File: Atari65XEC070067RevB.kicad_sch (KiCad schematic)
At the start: 192 parts, among them J7 DIN-7, Q1 2N3904, Q2 2N3904, Q3 2N3904, Q4 2N3904, Q5 2N3904, Q6 2N3904, SW1 SW_SPDT, U1 LM358, U17 GTIA, U18 74LS08, U19 NE555P, U20 4050, U21 74LS74, U22 POKEY, U23 6520, U24 4051, U25 4051, U34 MMMU, U35 74LS95, U4 BASIC, U5 OS ROM, U6 SALLY, U7 ANTIC, Y2 4.33618MHz

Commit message: add ports
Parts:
- added C63, C64, C65, C66, C71, C72, C73, C74, C75, C76, C77, C78, C82, C83, C84, C85, C86, C87, C88, C89, C90, C91, C92, C96, C97: 1nF, symbol Device:C_Small
- added C68, C69, C70, C93: 100nF, symbol Device:C_Small
- added C94, C95: 10nF, symbol Device:C_Small
- added CR5: ~, symbol Device:D_Small
- added J1: SIO, symbol Library:SIO
- added J1: ~, symbol Library:KEYBOARD
- added J2: MONITOR, symbol Connector:DIN-5_180degree
- added J5, J6: JOY1, symbol Connector:DE9_Socket
- added L102, L23, L30, L31: FB, symbol Device:L_Ferrite
- added L14: 22uH, symbol Device:L_Ferrite
- added L15, L16, L17, L18, L19, L20, L21, L22, L24, L26, L27, L28, L29: 10uH, symbol Device:L_Ferrite
- added Q7: MPSA55, PCM_Package_TO_SOT_THT_AKL:TO-92_Inline_Wide_EBC, symbol PCM_Transistor_BJT_AKL:MPSA56
- added R117, R118, R119: 100R, symbol Device:R_Small
- added R120, R121, R122, R123, R124, R125, R126, R127, R132, R133, R134, R135, R136, R95: 220R, symbol Device:R_Small
- added R128, R129, R130, R131, R90: 100, symbol Device:R_Small
- added R137, R138, R139, R140, R141, R142, R143, R144, R145, R146, R147, R148, R149, R150, R151, R152, R153: 270R, symbol Device:R_Small
- added R205: 150R, symbol Device:R_Small
- added R74, R75, R85, R86: 3k, symbol Device:R_Small
- added R76, R77, R78, R79: 1k8, symbol Device:R_Small
- added R81, R82, R83, R84, R92, R93, R94: 4k7, symbol Device:R_Small
- added R89, R96: 47k, symbol Device:R_Small
- added R91: 2k7, symbol Device:R_Small
- added W1: ~, symbol Jumper:Jumper_2_Bridged
- renumbered JA4 to J4A, JB4 to J4B, R1 to R21, YA1 to Y1, YB1 to Y1B
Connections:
- net +5VA: now also C112.1, C19.1, U23.20 (VCC), U24.16 (VCC), U25.16 (VCC), C68.2, C69.1, C70.1, C93.2, C94.1, CR5.1 (K), J1.1, J1.10, J1.11, J1.12, Q7.1 (E), R74.2, R75.2, R81.2, R82.2, R83.2, R84.2, R85.1, R86.1, R89.1, R92.2, R93.2, R94.2, R95.2, R96.2
- net +5VD: now also C1.2, C10.2, C102.1, C103.2, C104.2, C105.1, C11.2, C112.2, C12.2, C13.2, C14.2, C15.2, C16.2, C18.2, C2.2, C201.1, C204.2, C205.2, C206.1, C21.2, C24.2, C25.2, C26.2, C27.2, C28.2, C29.1, C3.2, C30.2, C32.2, C33.2, C4.2, C42.2, C46.1, C47.1, C48.1, C5.2, C50.2, C51.1, C58.1, C6.2, C60.1, C61.1, C62.1, C7.2, C8.2, C9.2, C98.2, C99.1, J4A.8 (GND), J4B.H (GND), J7.3, J7.5, J7.7, Q1.1 (E), Q6.1 (E), R10.1, R11.2, R13.1, R14.1, R18.2, R200.1, R202.1, R27.2, R29.2, R3.1, R38.3, R52.1, R53.1, R69.1, U1.4 (V-), U10.16 (GND), U11.16 (GND), U12.16 (GND), U13.16 (GND), U14.16 (GND), U15.16 (GND), U16.16 (GND), U17.3 (GND), U18.7 (GND), U19.1 (GND), U2.5 (E2), U2.8 (GND), U20.8 (VSS), U21.7 (GND), U22.1 (GND), U22.11 (P5), U22.8 (P6), U22.9 (P7), U23.1 (VSS), U24.6 (Inh), U24.7 (VEE), U24.8 (VSS), U25.6 (Inh), U25.7 (VEE), U25.8 (VSS), U26.16 (GND), U27.16 (GND), U28.16 (GND), U29.16 (GND), U3.10 (GND), U30.16 (GND), U31.16 (GND), U32.16 (GND), U33.16 (GND), U34.10 (GND), U34.7 (NC), U34.8 (NC), U34.9 (NC), U35.12 (QB), U35.3 (B), U35.4 (C), U35.6 (Mode), U35.7 (GND), U35.8 (CLK2), U4.12 (GND), U5.14 (GND), U6.1 (GND), U6.21 (GND), U6.38 (S0), U7.1 (GND), U8.20 (GND), U9.16 (GND), Y1B.7 (GND), C63.1, C64.1, C65.1, C66.1, C68.1, C69.2, C70.2, C71.1, C72.1, C73.1, C74.1, C75.1, C76.1, C77.1, C78.1, C82.1, C82.2, C83.1, C83.2, C84.1, C84.2, C85.1, C86.1, C87.1, C88.1, C89.1, C90.1, C91.1, C92.1, C93.1, C94.2, C95.1, C96.1, C97.1, J1.13, J1.3, J1.4, J1.6, J1.7, J1.9, J2.2, L102.1, L24.2, R117.2, R118.2, R119.2, R90.1, W1.2 (B)
- net at R40.2: now also L14.2
- net at Q2.1 (E), R202.2: now also R205.1
- net at L7.2: now also J2.4
- net at U3.18 (~{BE}): now also U23.11 (PB1), R85.2
- net at U17.12 (S0): now also R134.1
- net at U17.13 (S1): now also R135.1
- net at U17.14 (S2): now also R136.1
- net at U17.8 (T0), U18.12: now also R132.1
- net at U17.9 (T1), U18.13: now also R133.1
- net at U23.18 (CB1): now also R118.1, R93.1
- net at U23.19 (CB2): now also R119.1, R94.1
- net at U23.2 (PA0): now also R120.1
- net at U23.22 (CS0): now also U23.24 (CS1), R86.2
- net at U23.3 (PA1): now also R121.1
- net at U23.39 (CA2): now also R91.1
- net at U23.4 (PA2): now also R122.1
- net at U23.40 (CA1): now also R117.1, R92.1
- net at U23.5 (PA3): now also R123.1
- net at U23.6 (PA4): now also R124.1
- net at U23.7 (PA5): now also R125.1
- net at U23.8 (PA6): now also R126.1
- net at U23.9 (PA7): now also R127.1
- net at U22.10 (P4): now also R75.1, W1.1 (A)
- net at U22.12 (P2): now also C66.2, R79.1
- net at U22.13 (P3): now also C63.2, R78.1
- net at U22.14 (P0): now also C65.2, R77.1
- net at U22.15 (P1): now also C64.2, R76.1
- net at U22.16 (~{KR2}): now also CR5.2 (A), R137.1, R96.1
- net at U22.18 (~{K5}): now also U25.9 (C)
- net at U22.19 (~{K4}): now also U25.10 (B)
- net at U22.20 (~{K3}): now also U25.11 (A)
- net at U22.21 (~{K2}): now also U24.9 (C)
- net at U22.22 (~{K1}): now also U24.10 (B)
- net at U22.23 (~{K0}): now also U24.11 (A)
- net at U22.24 (SID): now also R130.1, R83.1
- net at U22.25 (~{KR1}): now also U24.3 (X), R89.2
- net at U22.26 (BCLK): now also R129.1, R82.1
- net at U22.27 (ACLK): now also R128.1, R81.1
- net at U22.28 (SOD): now also R131.1, R84.1
- net at U22.31 (CS1): now also R74.1
- net at R10.2, R8.1: now also J2.3
- net at U25.1 (X4): now also R141.1
- net at U25.12 (X3): now also R142.1
- net at U25.13 (X0): now also R145.1
- net at U25.14 (X1): now also R144.1
- net at U25.15 (X2): now also R143.1
- net at U25.2 (X6): now also R139.1
- net at U25.3 (X): now also R90.2
- net at U25.4 (X7): now also R138.1
- net at U25.5 (X5): now also R140.1
- net at U24.1 (X4): now also R150.1
- net at U24.12 (X3): now also R149.1
- net at U24.13 (X0): now also R146.1
- net at U24.14 (X1): now also R147.1
- net at U24.15 (X2): now also R148.1
- net at U24.2 (X6): now also R152.1
- net at U24.4 (X7): now also R153.1
- net at U24.5 (X5): now also R151.1
- net at L9.2: now also J2.1
- removed net GND: C1.2, C10.2, C102.1, C103.2, C104.2, C105.1, C11.2, C112.2, C12.2, C13.2, C14.2, C15.2, C16.2, C18.2, C2.2, C201.1, C204.2, C205.2, C206.1, C21.2, C24.2, C25.2, C26.2, C27.2, C28.2, C29.1, C3.2, C30.2, C32.2, C33.2, C4.2, C42.2, C46.1, C47.1, C48.1, C5.2, C50.2, C51.1, C58.1, C6.2, C60.1, C61.1, C62.1, C7.2, C8.2, C9.2, C98.2, C99.1, J4A.8 (GND), J4B.H (GND), J7.3, J7.5, J7.7, Q1.1 (E), Q6.1 (E), R10.1, R11.2, R13.1, R14.1, R18.2, R200.1, R202.1, R27.2, R29.2, R3.1, R38.3, R52.1, R53.1, R69.1, U1.4 (V-), U10.16 (GND), U11.16 (GND), U12.16 (GND), U13.16 (GND), U14.16 (GND), U15.16 (GND), U16.16 (GND), U17.3 (GND), U18.7 (GND), U19.1 (GND), U2.5 (E2), U2.8 (GND), U20.8 (VSS), U21.7 (GND), U22.1 (GND), U26.16 (GND), U27.16 (GND), U28.16 (GND), U29.16 (GND), U3.10 (GND), U30.16 (GND), U31.16 (GND), U32.16 (GND), U33.16 (GND), U34.10 (GND), U34.7 (NC), U34.8 (NC), U34.9 (NC), U35.12 (QB), U35.3 (B), U35.4 (C), U35.6 (Mode), U35.7 (GND), U35.8 (CLK2), U4.12 (GND), U5.14 (GND), U6.1 (GND), U6.21 (GND), U6.38 (S0), U7.1 (GND), U8.20 (GND), U9.16 (GND), Y1B.7 (GND)
- new net: J1.14, R141.2
- new net: J1.11, R147.2
- new net: J1.21 (START), R136.2
- new net: C87.2, L27.1, R122.2
- new net: C91.2, L20.1, R126.2
- new net: C89.2, L22.1, R124.2
- new net: J5.1, L22.2
- new net: J1.19, R150.2
- new net: J1.7, R138.2
- new net: C75.2, J1.2, R128.2
- new net: J6.3, L27.2
- new net: J5.3, L20.2
- new net: J1.16, R149.2
- new net: J1.23 (OPTION), R134.2
- new net: C72.2, L18.1, R77.2
- new net: J6.9, L18.2
- new net: C74.2, L16.1, R79.2
- new net: C78.2, J1.5, R131.2
- new net: C97.2, L30.1, R132.2
- new net: J6.6, L30.2
- new net: C71.2, L17.1, R76.2
- new net: C73.2, L15.1, R78.2
- new net: J5.5, L15.2
- new net: J6.5, L17.2
- new net: J1.22 (SELECT), R135.2
- new net: J1.20, R137.2
- new net: J6.1, L29.2
- new net: J6.2, L28.2
- new net: J6.4, L26.2
- new net: J5.7, J6.7, L102.2
- new net: J5.8, J6.8, L24.1
- new net: C85.2, L29.1, R120.2
- new net: J1.5, R142.2
- new net: C90.2, L21.1, R125.2
- new net: J1.9, R153.2
- new net: C77.2, J1.3, R130.2
- new net: C86.2, L28.1, R121.2
- new net: C76.2, J1.1, R129.2
- new net: J1.8, Q7.3 (C)
- new net: L31.1, R205.2
- new net: J2.5, L31.2
- new net: J1.13, R144.2
- new net: J1.17, R146.2
- new net: J5.2, L21.2
- new net: J1.15, R143.2
- new net: Q7.2 (B), R91.2
- new net: C96.2, L23.1, R133.2
- new net: J5.9, L16.2
- new net: J1.10, R151.2
- new net: J1.12, R139.2
- new net: J1.18, R145.2
- new net: C95.2, J1.2, R95.1
- new net: J1.24 (RESET), L14.1
- new net: J1.4, R152.2
- new net: J1.6, R140.2
- new net: J1.8, R148.2
- new net: J5.4, L19.2
- new net: J5.6, L23.2
- new net: C92.2, L19.1, R127.2
- new net: C88.2, L26.1, R123.2
- no-connect marks 11 -> 13
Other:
- note removed: "+5D appears to be a typo"
- moved on the sheet: R206, R23, R24, R25, U23, U24, U25

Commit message: complete schematic
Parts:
- added C301, C302, C303, C304: 27pF, symbol Device:C_Small
- added C305, C306, C307, C308, C309, C310, C80, C81: 1nF, symbol Device:C_Small
- added C79: 22uF, symbol Device:C_Polarized_Small
- added L10, L11: FB, symbol Device:L_Ferrite
- C19, C20, C22: value 4u7 -> 4u7^{*}
- J8: renamed from J1; value ~ -> KEYBOARD
- renumbered J4A to JA4, J4B to JB4, L102 to L103, R21 to R1, Y1 to YA1, Y1B to YB1
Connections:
- net +5VA: now also L10.1; no longer C112.1, C19.1, J1.10, J1.11, J1.12
- net +5VD: now also C301.1, C302.1, C303.1, C304.1, C305.1, C305.2, C306.1, C307.1, C307.2, C308.1, C309.1, C310.1, C310.2, C80.1, C81.1
- net Shield: now also C79.2
- net S2: now reaches R136.1, U17.14 (S2)
- net CLOCK_OUT: now reaches C75.2, J1.2, R128.2
- net CLOCK_OUT: now also C301.2
- net HALT: now reaches JB4.C (HALT), U17.26 (HALT), U34.13 (HALT), U35.1 (SDI), U6.35 (~{HALT}), U7.9 (~{HALT})
- net BO2: now reaches JA4.S (B02), U17.30 (O2), U18.3, U22.7 (O2), U23.25 (O2), U34.19 (O2), U35.9 (CLK1), U7.29 (O2), U8.5 (O2)
- net RW: now reaches JA4.R (R/~{W}), U17.33 (R/~{W}), U22.32 (R/~{W}), U23.21 (R/~{W}), U6.36 (R/~{W}), U8.38 (R/~{W})
- net COMPOSITE: now reaches J2.4, L7.2
- net S0: now reaches R134.1, U17.12 (S0)
- net S1: now reaches R135.1, U17.13 (S1)
- net T0: now reaches R132.1, U17.8 (T0), U18.12
- net T1: now reaches R133.1, U17.9 (T1), U18.13
- net P0: now reaches J6.9, L18.2
- net DATA_OUT: now reaches C78.2, J1.5, R131.2
- net DATA_OUT: now also C304.2
- net IRQ: now reaches JB4.B (~{IRQ}), R21.1, R22.1, U22.29 (~{IRQ}), U23.37 (~{IRQB}), U23.38 (~{IRQA}), U6.4 (~{IRQ}), U6.6 (~{NMI}), U7.7 (~{NMI})
- net P3: now reaches J5.5, L15.2
- net P1: now reaches J6.5, L17.2
- net DATA_IN: now reaches C77.2, J1.3, R130.2
- net DATA_IN: now also C303.2
- net MONITOR_AUDIO: now reaches J2.3, R10.2, R8.1
- net CLOCK_IN: now reaches C76.2, J1.1, R129.2
- net CLOCK_IN: now also C302.2
- net at Q7.3 (C): now also L11.1; no longer J1.8
- net CHROMA: now reaches J2.5, L31.2
- net P2: now reaches J5.9, L16.2
- net LUMA: now reaches J2.1, L9.2
- new net MOTOR_CONTROL: C306.2, C81.2, J1.8, L11.2
- new net READY_+5V: C308.2, C79.1, C80.2, J1.10, L10.2
- new net SIO_AUDIO: C112.1, C19.1, C309.2, J1.11
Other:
- note added: "^{*}C19, C20, C22 are non-polarized"
- title: 65XE 070067 -> 65XE/130XE C070065/C070067 rev-B

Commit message: start layout
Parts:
- added C113, C114, C115, C116, C117, C118, C119, C120, C34, C35, C36, C37, C38, C39, C40, C41: 100nF, Capacitor_THT:C_Axial_L3.8mm_D2.6mm_P10.00mm_Horizontal, symbol Device:C_Small
- C1, C10, C2, C24, C3, C50, C79: footprint (none) -> Capacitor_THT:CP_Radial_D8.0mm_P5.00mm
- C102, C103, C104, C105, C11, C111, C112, C12, C13, C14, C15, C16, C17, C18, C200, C201, C204, C205, C206, C21, C23, C25, C26, C27, C28, C29, C30, C301, C302, C303, C304, C305, C306, C307, C308, C309, C31, C310, C32, C33, C4, C42, C44, C46, C47, C48, C5, C51, C58, C59, C6, C60, C61, C62, C63, C64, C65, C66, C68, C69, C7, C70, C71, C72, C73, C74, C75, C76, C77, C78, C8, C80, C81, C82, C83, C84, C85, C86, C87, C88, C89, C9, C90, C91, C92, C93, C94, C95, C96, C97, C98, C99: footprint (none) -> Capacitor_THT:C_Axial_L3.8mm_D2.6mm_P12.50mm_Horizontal
- C19, C20, C22: footprint (none) -> Capacitor_THT:CP_Radial_D5.0mm_P2.50mm
- CR2, CR3, CR4, CR5: footprint (none) -> Diode_THT:D_DO-35_SOD27_P12.70mm_Horizontal
- J5, J6: footprint (none) -> Connector_Dsub:DSUB-9_Pins_Horizontal_P2.77x2.54mm_EdgePinOffset9.40mm
- L1, L10, L102, L11, L12, L13, L14, L15, L16, L17, L18, L19, L2, L20, L21, L22, L23, L24, L25, L26, L27, L28, L29, L3, L30, L31, L32, L37, L5, L6, L7, L8, L9: footprint (none) -> Inductor_THT:L_Axial_L7.0mm_D3.3mm_P12.70mm_Horizontal_Fastron_MICC
- L101: renamed from L103; footprint (none) -> Inductor_THT:L_Axial_L7.0mm_D3.3mm_P12.70mm_Horizontal_Fastron_MICC
- L103: renamed from L10; footprint (none) -> Inductor_THT:L_Axial_L7.0mm_D3.3mm_P12.70mm_Horizontal_Fastron_MICC
- R1, R10, R11, R110, R111, R116, R117, R118, R119, R12, R120, R121, R122, R123, R124, R125, R126, R127, R128, R129, R13, R130, R131, R132, R133, R134, R135, R136, R137, R138, R139, R14, R140, R141, R142, R143, R144, R145, R146, R147, R148, R149, R15, R150, R151, R152, R153, R18, R19, R2, R20, R200, R201, R202, R203, R204, R205, R206, R21, R22, R23, R24, R25, R26, R27, R28, R29, R3, R30, R31, R33, R34, R35, R36, R37, R38, R39, R4, R40, R41, R42, R43, R44, R45, R46, R47, R48, R49, R5, R50, R51, R52, R53, R6, R69, R7, R70, R71, R72, R73, R74, R75, R76, R77, R78, R79, R8, R80, R81, R82, R83, R84, R85, R86, R87, R89, R9, R90, R91, R92, R93, R94, R95, R96, W2: footprint (none) -> Resistor_THT:R_Axial_DIN0309_L9.0mm_D3.2mm_P12.70mm_Horizontal
- U1: footprint (none) -> Package_DIP:DIP-8_W7.62mm
- U10, U11, U12, U13, U14, U15, U16, U26, U27, U28, U29, U30, U31, U32, U33, U9: value ~ -> 4164; footprint (none) -> Package_DIP:DIP-16_W7.62mm
- U17, U6, U7: footprint (none) -> Package_DIP:DIP-40_W15.24mm
- U18, U21, U35: footprint (none) -> Package_DIP:DIP-14_W7.62mm
- U2: value ~ -> 74LS138; footprint (none) -> Package_DIP:DIP-16_W7.62mm
- U20, U24, U25: footprint (none) -> Package_DIP:DIP-16_W7.62mm
- U3: value ~ -> 4164; footprint (none) -> Package_DIP:DIP-20_W7.62mm
- U34: footprint (none) -> Package_DIP:DIP-20_W7.62mm
- U4: footprint (none) -> Package_DIP:DIP-24_W15.24mm
- U5: footprint (none) -> Package_DIP:DIP-28_W15.24mm
- U8: value ~ -> FREDDIE; footprint (none) -> Package_DIP:DIP-40_W15.24mm
- W1: value ~ -> Jumper_2_Closed; footprint (none) -> Resistor_THT:R_Axial_DIN0309_L9.0mm_D3.2mm_P12.70mm_Horizontal
- Y2: footprint (none) -> Crystal:Crystal_HC49-U_Horizontal
- YA1: value ~ -> See Note; footprint (none) -> Crystal:Crystal_HC49-U_Horizontal
- YB1: value ~ -> See Note; footprint (none) -> Oscillator:Oscillator_DIP-14
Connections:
- net +5VA: now also C113.1, C114.1, C115.1, C116.1, C117.1, C118.1, C119.1, C120.1, C34.1, C35.1, C36.1, C37.1, C38.1, C39.1, C40.1, C41.1
- net +5VD: now also C113.2, C114.2, C115.2, C116.2, C117.2, C118.2, C119.2, C120.2, C34.2, C35.2, C36.2, C37.2, C38.2, C39.2, C40.2, C41.2

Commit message: initial pcb layout
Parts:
- U3: value 4164 -> MMU
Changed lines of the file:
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@@
 			)
 		)
-		(property "Value" "4164"
+		(property "Value" "MMU"
 			(at 97.79 229.87 0)
 			(effects

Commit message: locate dram and trace around it
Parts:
- C102, C103, C104, C105, C11, C111, C112, C12, C13, C14, C15, C16, C17, C18, C200, C201, C204, C205, C206, C21, C23, C25, C26, C27, C28, C29, C30, C31, C32, C33, C4, C42, C44, C46, C47, C48, C5, C51, C58, C59, C6, C60, C61, C62, C63, C64, C65, C66, C68, C69, C7, C70, C71, C72, C73, C74, C75, C76, C77, C78, C8, C80, C81, C82, C83, C84, C85, C86, C87, C88, C89, C9, C90, C91, C92, C93, C94, C95, C96, C97, C98, C99: footprint Capacitor_THT:C_Axial_L3.8mm_D2.6mm_P12.50mm_Horizontal -> Library:C_Axial_L5.1mm_D2.7mm_P12.72mm_Horizontal
- C113, C114, C115, C116, C117, C118, C119, C120, C34, C35, C36, C37, C38, C39, C40, C41: footprint Capacitor_THT:C_Axial_L3.8mm_D2.6mm_P10.00mm_Horizontal -> Library:C_Axial_L3.8mm_D2.6mm_P10.16mm_Horizontal
- C19, C20, C22: footprint Capacitor_THT:CP_Radial_D5.0mm_P2.50mm -> Library:CE_NP_Radial_D8.0mm_P2.50mm
- C301, C302, C303, C304, C305, C306, C307, C308, C309, C310: footprint Capacitor_THT:C_Axial_L3.8mm_D2.6mm_P12.50mm_Horizontal -> Capacitor_THT:C_Disc_D3.0mm_W1.6mm_P2.50mm; now not fitted
- J2: footprint (none) -> Library:CUI_SDS-50J
- R1, R10, R11, R110, R111, R116, R117, R118, R119, R12, R120, R121, R122, R123, R124, R125, R126, R127, R128, R129, R13, R130, R131, R132, R133, R134, R135, R136, R137, R138, R139, R14, R140, R141, R142, R143, R144, R145, R146, R147, R148, R149, R15, R150, R151, R152, R153, R18, R19, R2, R20, R200, R201, R202, R203, R204, R205, R206, R21, R22, R23, R24, R25, R26, R27, R28, R29, R3, R30, R31, R33, R34, R35, R36, R37, R39, R4, R40, R41, R42, R43, R44, R45, R46, R47, R48, R49, R5, R50, R51, R52, R53, R6, R69, R7, R70, R71, R72, R73, R74, R75, R76, R77, R78, R79, R8, R80, R81, R82, R83, R84, R85, R86, R87, R89, R9, R90, R91, R92, R93, R94, R95, R96: footprint Resistor_THT:R_Axial_DIN0309_L9.0mm_D3.2mm_P12.70mm_Horizontal -> Library:R_Axial_L9.0mm_D2.7mm_P12.70mm_Horizontal
- R38: footprint Resistor_THT:R_Axial_DIN0309_L9.0mm_D3.2mm_P12.70mm_Horizontal -> Potentiometer_THT:Potentiometer_Runtron_RM-065_Vertical
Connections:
- net Shield is gone; now on net GND: C79.2, J7.2
- net +5VA: now also C113.2, C114.2, C115.2, C116.2, C117.2, C118.2, C119.2, C120.2, C34.2, C35.2, C36.2, C37.2, C38.2, C39.2, C40.2, C41.2, R23.1, R24.1, R25.1; no longer C113.1, C114.1, C115.1, C116.1, C117.1, C118.1, C119.1, C120.1, C34.1, C35.1, C36.1, C37.1, C38.1, C39.1, C40.1, C41.1, R23.2, R24.2, R25.2
- net +5VD: no longer C1.2, C10.2, C102.1, C103.2, C104.2, C105.1, C11.2, C112.2, C113.2, C114.2, C115.2, C116.2, C117.2, C118.2, C119.2, C12.2, C120.2, C13.2, C14.2, C15.2, C16.2, C18.2, C2.2, C201.1, C204.2, C205.2, C206.1, C21.2, C24.2, C25.2, C26.2, C27.2, C28.2, C29.1, C3.2, C30.2, C301.1, C302.1, C303.1, C304.1, C305.1, C305.2, C306.1, C307.1, C307.2, C308.1, C309.1, C310.1, C310.2, C32.2, C33.2, C34.2, C35.2, C36.2, C37.2, C38.2, C39.2, C4.2, C40.2, C41.2, C42.2, C46.1, C47.1, C48.1, C5.2, C50.2, C51.1, C58.1, C6.2, C60.1, C61.1, C62.1, C63.1, C64.1, C65.1, C66.1, C68.1, C69.2, C7.2, C70.2, C71.1, C72.1, C73.1, C74.1, C75.1, C76.1, C77.1, C78.1, C8.2, C80.1, C81.1, C82.1, C82.2, C83.1, C83.2, C84.1, C84.2, C85.1, C86.1, C87.1, C88.1, C89.1, C9.2, C90.1, C91.1, C92.1, C93.1, C94.2, C95.1, C96.1, C97.1, C98.2, C99.1, J1.13, J1.4, J1.6, J1.7, J1.9, J2.2, J7.3, J7.5, J7.7, J8.3, JA4.8 (GND), JB4.H (GND), L24.2, Q1.1 (E), Q6.1 (E), R10.1, R11.2, R117.2, R118.2, R119.2, R13.1, R14.1, R18.2, R200.1, R202.1, R27.2, R29.2, R3.1, R38.3, R52.1, R53.1, R69.1, R90.1, U1.4 (V-), U10.16 (GND), U11.16 (GND), U12.16 (GND), U13.16 (GND), U14.16 (GND), U15.16 (GND), U16.16 (GND), U17.3 (GND), U18.7 (GND), U19.1 (GND), U2.5 (E2), U2.8 (GND), U20.8 (VSS), U21.7 (GND), U22.1 (GND), U22.11 (P5), U22.8 (P6), U22.9 (P7), U23.1 (VSS), U24.6 (Inh), U24.7 (VEE), U24.8 (VSS), U25.6 (Inh), U25.7 (VEE), U25.8 (VSS), U26.16 (GND), U27.16 (GND), U28.16 (GND), U29.16 (GND), U3.10 (GND), U30.16 (GND), U31.16 (GND), U32.16 (GND), U33.16 (GND), U34.10 (GND), U34.7 (NC), U34.8 (NC), U34.9 (NC), U35.12 (QB), U35.3 (B), U35.4 (C), U35.6 (Mode), U35.7 (GND), U35.8 (CLK2), U4.12 (GND), U5.14 (GND), U6.1 (GND), U6.21 (GND), U6.38 (S0), U7.1 (GND), U8.20 (GND), U9.16 (GND), W1.2 (B), YB1.7 (GND)
- net at U23.14 (PB4), U34.5 (CBE): now also R24.2; no longer R24.1
- net at U23.12 (PB2), U34.3 (BA14): now also R25.2; no longer R25.1
- net at U23.13 (PB3), U34.4 (BA15): now also R23.2; no longer R23.1
- net at U29.15 (~{CAS}): now also R111.2, U26.15 (~{CAS}), U27.15 (~{CAS}), U28.15 (~{CAS}), U30.15 (~{CAS}), U31.15 (~{CAS}), U32.15 (~{CAS}), U33.15 (~{CAS})
- net GND: now reaches U35.2 (A)
- net GND: now also C1.2, C10.2, C102.1, C103.2, C104.2, C105.1, C11.2, C112.2, C113.1, C114.1, C115.1, C116.1, C117.1, C118.1, C119.1, C12.2, C120.1, C13.2, C14.2, C15.2, C16.2, C18.2, C2.2, C201.1, C204.2, C205.2, C206.1, C21.2, C24.2, C25.2, C26.2, C27.2, C28.2, C29.1, C3.2, C30.2, C301.1, C302.1, C303.1, C304.1, C305.1, C305.2, C306.1, C307.1, C307.2, C308.1, C309.1, C310.1, C310.2, C32.2, C33.2, C34.1, C35.1, C36.1, C37.1, C38.1, C39.1, C4.2, C40.1, C41.1, C42.2, C46.1, C47.1, C48.1, C5.2, C50.2, C51.1, C58.1, C6.2, C60.1, C61.1, C62.1, C63.1, C64.1, C65.1, C66.1, C68.1, C69.2, C7.2, C70.2, C71.1, C72.1, C73.1, C74.1, C75.1, C76.1, C77.1, C78.1, C8.2, C80.1, C81.1, C82.1, C82.2, C83.1, C83.2, C84.1, C84.2, C85.1, C86.1, C87.1, C88.1, C89.1, C9.2, C90.1, C91.1, C92.1, C93.1, C94.2, C95.1, C96.1, C97.1, C98.2, C99.1, J1.13, J1.4, J1.6, J1.7, J1.9, J2.2, J7.3, J7.5, J7.7, J8.3, JA4.8 (GND), JB4.H (GND), L24.2, Q1.1 (E), Q6.1 (E), R10.1, R11.2, R117.2, R118.2, R119.2, R13.1, R14.1, R18.2, R200.1, R202.1, R27.2, R29.2, R3.1, R38.3, R52.1, R53.1, R69.1, R90.1, U1.4 (V-), U10.16 (GND), U11.16 (GND), U12.16 (GND), U13.16 (GND), U14.16 (GND), U15.16 (GND), U16.16 (GND), U17.3 (GND), U18.7 (GND), U19.1 (GND), U2.5 (E2), U2.8 (GND), U20.8 (VSS), U21.7 (GND), U22.1 (GND), U22.11 (P5), U22.8 (P6), U22.9 (P7), U23.1 (VSS), U24.6 (Inh), U24.7 (VEE), U24.8 (VSS), U25.6 (Inh), U25.7 (VEE), U25.8 (VSS), U26.16 (GND), U27.16 (GND), U28.16 (GND), U29.16 (GND), U3.10 (GND), U30.16 (GND), U31.16 (GND), U32.16 (GND), U33.16 (GND), U34.10 (GND), U34.7 (NC), U34.8 (NC), U34.9 (NC), U35.12 (QB), U35.3 (B), U35.4 (C), U35.5 (D), U35.6 (Mode), U35.7 (GND), U35.8 (CLK2), U4.12 (GND), U5.14 (GND), U6.1 (GND), U6.21 (GND), U6.38 (S0), U7.1 (GND), U8.20 (GND), U9.16 (GND), W1.2 (B), YB1.7 (GND)
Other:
- note added: "Technically only bridged on top of board"
- moved on the sheet: C113, C114, C115, C116, C117, C118, C119, C120, C34, C35, C36, C37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

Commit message: progress routing
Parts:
- U17: value GTIA -> C014889/GTIA
- U22: value POKEY -> C012294/POKEY
- U23: value 6520 -> C014795 PIA/6520
- U6: value SALLY -> CO14806/SALLY
- U7: value ANTIC -> C021698/ANTIC
- U8: value FREDDIE -> C061991/FREDDIE
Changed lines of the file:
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@@
 			)
 		)
-		(property "Value" "GTIA"
-			(at 260.604 139.192 0)
+		(property "Value" "C014889/GTIA"
+			(at 266.7 109.474 90)
 			(effects
 				(font
@@
 		(on_board yes)
 		(dnp no)
-		(fields_autoplaced yes)
 		(property "Reference" "U23"
-			(at 447.04 111.76 0)
+			(at 447.04 115.062 0)
 			(effects
 				(font
@@
 			)
 		)
-		(property "Value" "6520"
-			(at 447.04 114.3 0)
+		(property "Value" "C014795 PIA/6520"
+			(at 446.786 159.512 90)
 			(effects
 				(font
@@
 		(on_board yes)
 		(dnp no)
-		(fields_autoplaced yes)
 		(property "Reference" "U22"
 			(at 372.11 285.75 0)
@@
 			)
 		)
-		(property "Value" "POKEY"
-			(at 372.11 288.29 0)
+		(property "Value" "C012294/POKEY"
+			(at 372.11 341.63 90)
 			(effects
 				(font
@@
 			)
 		)
-		(property "Value" "SALLY"
+		(property "Value" "CO14806/SALLY"
 			(at 215.9 181.356 90)
 			(effects
@@
 			)
 		)
-		(property "Value" "FREDDIE"
-			(at 148.59 323.85 0)
+		(property "Value" "C061991/FREDDIE"
+			(at 148.59 275.59 90)
 			(effects
 				(font
@@
 			)
 		)
-		(property "Value" "ANTIC"
-			(at 215.9 88.646 0)
+		(property "Value" "C021698/ANTIC"
+			(at 216.154 110.49 90)
 			(effects
 				(font

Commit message: update progress
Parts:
- C24: footprint Capacitor_THT:CP_Radial_D8.0mm_P5.00mm -> Capacitor_THT:CP_Axial_L10.0mm_D4.5mm_P15.00mm_Horizontal
- C50: footprint Capacitor_THT:CP_Radial_D8.0mm_P5.00mm -> Capacitor_THT:CP_Radial_D5.0mm_P2.50mm
- renumbered C104 to C101
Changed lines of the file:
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@@
 			)
 		)
-		(property "Footprint" "Capacitor_THT:CP_Radial_D8.0mm_P5.00mm"
+		(property "Footprint" "Capacitor_THT:CP_Axial_L10.0mm_D4.5mm_P15.00mm_Horizontal"
 			(at 93.98 142.24 0)
 			(effects
@@
 		(on_board yes)
 		(dnp no)
-		(property "Reference" "C104"
+		(property "Reference" "C101"
 			(at 86.106 362.966 90)
 			(effects
@@
 			(project "Atari65XEC070067RevB"
 				(path "/87d66ada-8337-4a7e-bc00-d889029d79b8"
-					(reference "C104")
+					(reference "C101")
 					(unit 1)
 				)
@@
 			)
 		)
-		(property "Footprint" "Capacitor_THT:CP_Radial_D8.0mm_P5.00mm"
+		(property "Footprint" "Capacitor_THT:CP_Radial_D5.0mm_P2.50mm"
 			(at 356.87 59.69 0)
 			(effects

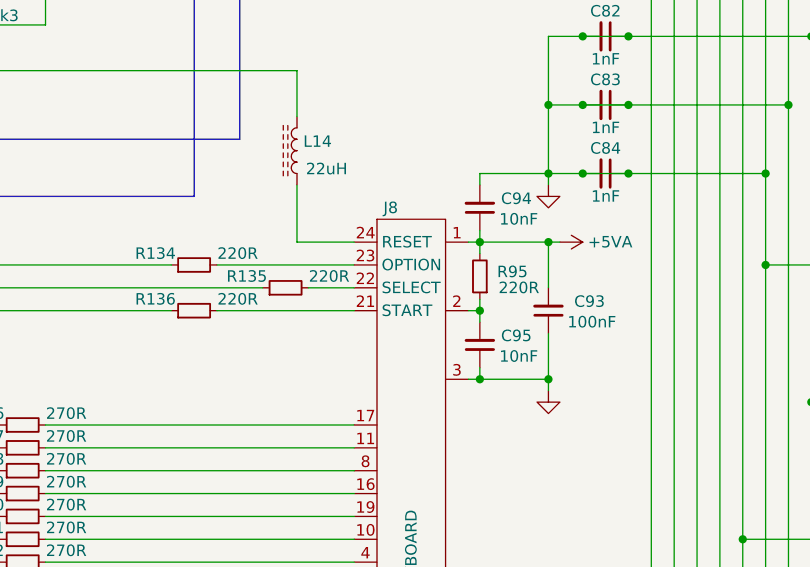
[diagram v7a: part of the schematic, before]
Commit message: correct wiring of control keys to GTIA
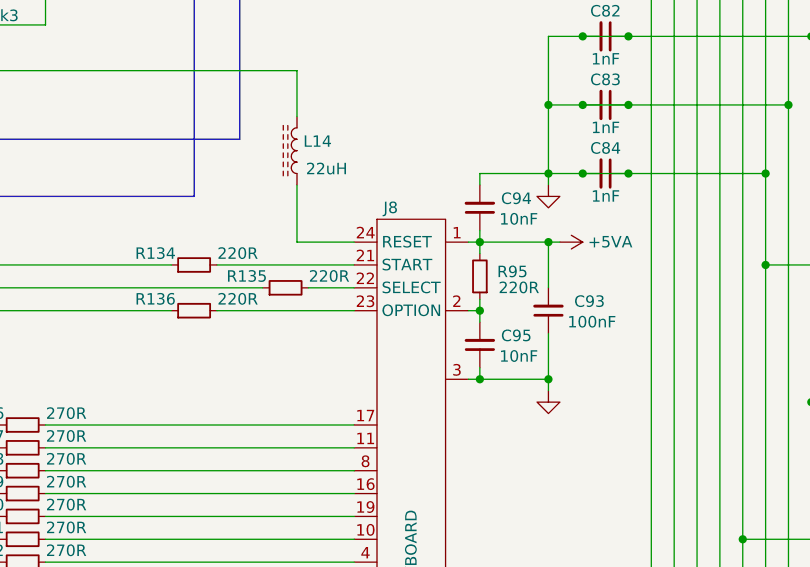
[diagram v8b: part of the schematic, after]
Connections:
- net at R136.2: now also J8.23 (OPTION); no longer J8.21 (START)
- net at R134.2: now also J8.21 (START); no longer J8.23 (OPTION)
